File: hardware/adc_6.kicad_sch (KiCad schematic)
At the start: 14 parts, among them J5 Conn_01x04, U5 ADS122C04IPW

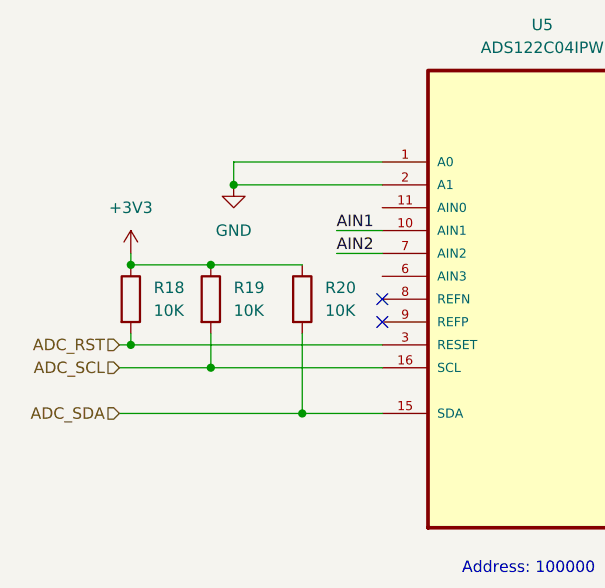
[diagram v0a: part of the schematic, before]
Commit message: Design Schematic for STM32F407
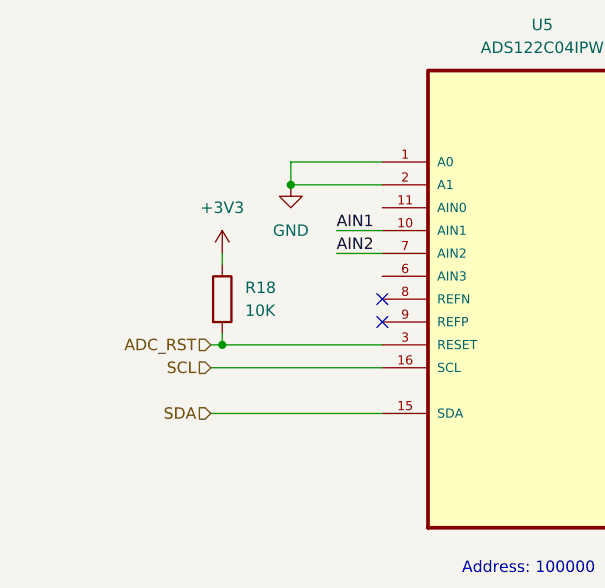
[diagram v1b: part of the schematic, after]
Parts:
- removed R19, R20: 10K, symbol Device:R
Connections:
- net ADC_SCL renamed SCL
- net ADC_SDA renamed SDA
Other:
- moved on the sheet: R18

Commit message: Complete Schematic for Power Section
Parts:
- renumbered C30 to C28, C31 to C29, C29 to C30, C32 to C31, C33 to C32, C34 to C33, R18 to R17, R21 to R18, R22 to R19
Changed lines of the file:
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@@
 		(dnp no)
 		(fields_autoplaced yes)
-		(property "Reference" "C31"
+		(property "Reference" "C29"
 			(at 176.53 100.3299 0)
 			(show_name no)
@@
 			(project "STM32F407 Dev Kit"
 				(path "/f3d27387-fbda-4c9d-aea0-93d92d34cd17/ffbc1d55-b358-41ae-b676-6d3702761bb2"
-					(reference "C31")
+					(reference "C29")
 					(unit 1)
 				)
@@
 		(dnp no)
 		(fields_autoplaced yes)
-		(property "Reference" "C33"
+		(property "Reference" "C32"
 			(at 199.39 109.2199 0)
 			(show_name no)
@@
 			(project "STM32F407 Dev Kit"
 				(path "/f3d27387-fbda-4c9d-aea0-93d92d34cd17/ffbc1d55-b358-41ae-b676-6d3702761bb2"
-					(reference "C33")
+					(reference "C32")
 					(unit 1)
 				)
@@
 		(dnp no)
 		(fields_autoplaced yes)
-		(property "Reference" "#PWR050"
+		(property "Reference" "#PWR051"
 			(at 165.1 87.63 0)
 			(hide yes)
@@
 			(project "STM32F407 Dev Kit"
 				(path "/f3d27387-fbda-4c9d-aea0-93d92d34cd17/ffbc1d55-b358-41ae-b676-6d3702761bb2"
-					(reference "#PWR050")
+					(reference "#PWR051")
 					(unit 1)
 				)
@@
 		(in_pos_files yes)
 		(dnp no)
-		(property "Reference" "R21"
+		(property "Reference" "R18"
 			(at 203.708 96.774 90)
 			(show_name no)
@@
 			(project "STM32F407 Dev Kit"
 				(path "/f3d27387-fbda-4c9d-aea0-93d92d34cd17/ffbc1d55-b358-41ae-b676-6d3702761bb2"
-					(reference "R21")
+					(reference "R18")
 					(unit 1)
 				)
@@
 		(dnp no)
 		(fields_autoplaced yes)
-		(property "Reference" "#PWR053"
+		(property "Reference" "#PWR048"
 			(at 149.86 120.65 0)
 			(hide yes)
@@
 			(project "STM32F407 Dev Kit"
 				(path "/f3d27387-fbda-4c9d-aea0-93d92d34cd17/ffbc1d55-b358-41ae-b676-6d3702761bb2"
-					(reference "#PWR053")
+					(reference "#PWR048")
 					(unit 1)
 				)
@@
 		(dnp no)
 		(fields_autoplaced yes)
-		(property "Reference" "#PWR034"
+		(property "Reference" "#PWR050"
 			(at 165.1 74.93 0)
 			(hide yes)
@@
 			(project "STM32F407 Dev Kit"
 				(path "/f3d27387-fbda-4c9d-aea0-93d92d34cd17/ffbc1d55-b358-41ae-b676-6d3702761bb2"
-					(reference "#PWR034")
+					(reference "#PWR050")
 					(unit 1)
 				)
@@
 		(dnp no)
 		(fields_autoplaced yes)
-		(property "Reference" "C29"
+		(property "Reference" "C30"
 			(at 177.8 62.2299 0)
 			(show_name no)
@@
 			(project "STM32F407 Dev Kit"
 				(path "/f3d27387-fbda-4c9d-aea0-93d92d34cd17/ffbc1d55-b358-41ae-b676-6d3702761bb2"
-					(reference "C29")
+					(reference "C30")
 					(unit 1)
 				)
@@
 		(dnp no)
 		(fields_autoplaced yes)
-		(property "Reference" "C30"
+		(property "Reference" "C28"
 			(at 168.91 74.9299 0)
 			(show_name no)
@@
 			(project "STM32F407 Dev Kit"
 				(path "/f3d27387-fbda-4c9d-aea0-93d92d34cd17/ffbc1d55-b358-41ae-b676-6d3702761bb2"
-					(reference "C30")
+					(reference "C28")
 					(unit 1)
 				)
@@
 		(dnp no)
 		(fields_autoplaced yes)
-		(property "Reference" "#PWR058"
+		(property "Reference" "#PWR053"
 			(at 184.15 121.92 0)
 			(hide yes)
@@
 			(project "STM32F407 Dev Kit"
 				(path "/f3d27387-fbda-4c9d-aea0-93d92d34cd17/ffbc1d55-b358-41ae-b676-6d3702761bb2"
-					(reference "#PWR058")
+					(reference "#PWR053")
 					(unit 1)
 				)
@@
 		(dnp no)
 		(fields_autoplaced yes)
-		(property "Reference" "#PWR052"
+		(property "Reference" "#PWR047"
 			(at 104.14 86.36 0)
 			(hide yes)
@@
 			(project "STM32F407 Dev Kit"
 				(path "/f3d27387-fbda-4c9d-aea0-93d92d34cd17/ffbc1d55-b358-41ae-b676-6d3702761bb2"
-					(reference "#PWR052")
+					(reference "#PWR047")
 					(unit 1)
 				)
@@
 		(dnp no)
 		(fields_autoplaced yes)
-		(property "Reference" "#PWR054"
+		(property "Reference" "#PWR046"
 			(at 96.52 91.44 0)
 			(hide yes)
@@
 			(project "STM32F407 Dev Kit"
 				(path "/f3d27387-fbda-4c9d-aea0-93d92d34cd17/ffbc1d55-b358-41ae-b676-6d3702761bb2"
-					(reference "#PWR054")
+					(reference "#PWR046")
 					(unit 1)
 				)
@@
 		(dnp no)
 		(fields_autoplaced yes)
-		(property "Reference" "#PWR059"
+		(property "Reference" "#PWR054"
 			(at 195.58 121.92 0)
 			(hide yes)
@@
 			(project "STM32F407 Dev Kit"
 				(path "/f3d27387-fbda-4c9d-aea0-93d92d34cd17/ffbc1d55-b358-41ae-b676-6d3702761bb2"
-					(reference "#PWR059")
+					(reference "#PWR054")
 					(unit 1)
 				)
@@
 		(in_pos_files yes)
 		(dnp no)
-		(property "Reference" "R22"
+		(property "Reference" "R19"
 			(at 203.708 104.14 90)
 			(show_name no)
@@
 			(project "STM32F407 Dev Kit"
 				(path "/f3d27387-fbda-4c9d-aea0-93d92d34cd17/ffbc1d55-b358-41ae-b676-6d3702761bb2"
-					(reference "R22")
+					(reference "R19")
 					(unit 1)
 				)
@@
 		(dnp no)
 		(fields_autoplaced yes)
-		(property "Reference" "C34"
+		(property "Reference" "C33"
 			(at 240.03 86.3599 0)
 			(show_name no)
@@
 			(project "STM32F407 Dev Kit"
 				(path "/f3d27387-fbda-4c9d-aea0-93d92d34cd17/ffbc1d55-b358-41ae-b676-6d3702761bb2"
-					(reference "C34")
+					(reference "C33")
 					(unit 1)
 				)
@@
 		(dnp no)
 		(fields_autoplaced yes)
-		(property "Reference" "#PWR051"
+		(property "Reference" "#PWR052"
 			(at 173.99 87.63 0)
 			(hide yes)
@@
 			(project "STM32F407 Dev Kit"
 				(path "/f3d27387-fbda-4c9d-aea0-93d92d34cd17/ffbc1d55-b358-41ae-b676-6d3702761bb2"
-					(reference "#PWR051")
+					(reference "#PWR052")
 					(unit 1)
 				)
@@
 		(dnp no)
 		(fields_autoplaced yes)
-		(property "Reference" "C32"
+		(property "Reference" "C31"
 			(at 187.96 109.2199 0)
 			(show_name no)
@@
 			(project "STM32F407 Dev Kit"
 				(path "/f3d27387-fbda-4c9d-aea0-93d92d34cd17/ffbc1d55-b358-41ae-b676-6d3702761bb2"
-					(reference "C32")
+					(reference "C31")
 					(unit 1)
 				)
@@
 		(dnp no)
 		(fields_autoplaced yes)
-		(property "Reference" "R18"
+		(property "Reference" "R17"
 			(at 99.06 91.4399 0)
 			(show_name no)
@@
 			(project "STM32F407 Dev Kit"
 				(path "/f3d27387-fbda-4c9d-aea0-93d92d34cd17/ffbc1d55-b358-41ae-b676-6d3702761bb2"
-					(reference "R18")
-					(unit 1)
-				)
+					(reference "R17")
+					(unit 1)
+				)

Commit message: Organize schematic
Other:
- note added: "ADC"
- note added: "Connector"
- moved on the sheet: C28, C29, C30, C31, C32, C33, FB2, J5, R17, R18, R19, U5

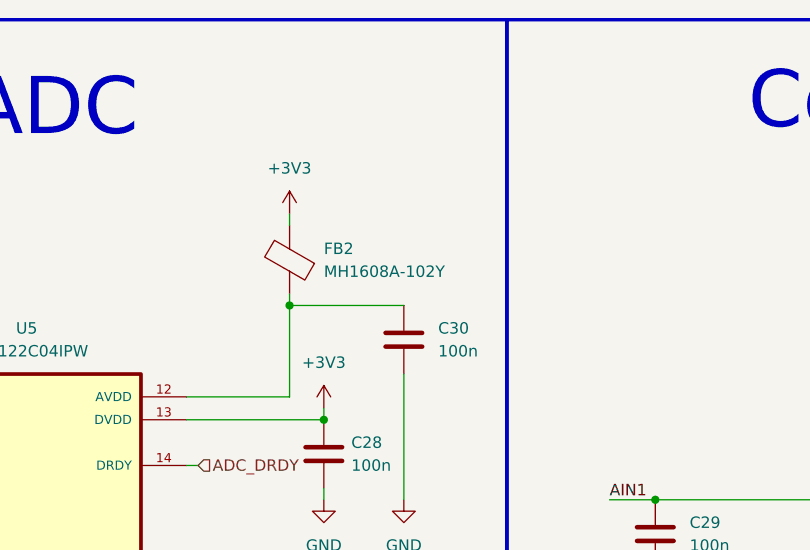
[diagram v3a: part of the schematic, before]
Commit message: Link footprints to Symbols
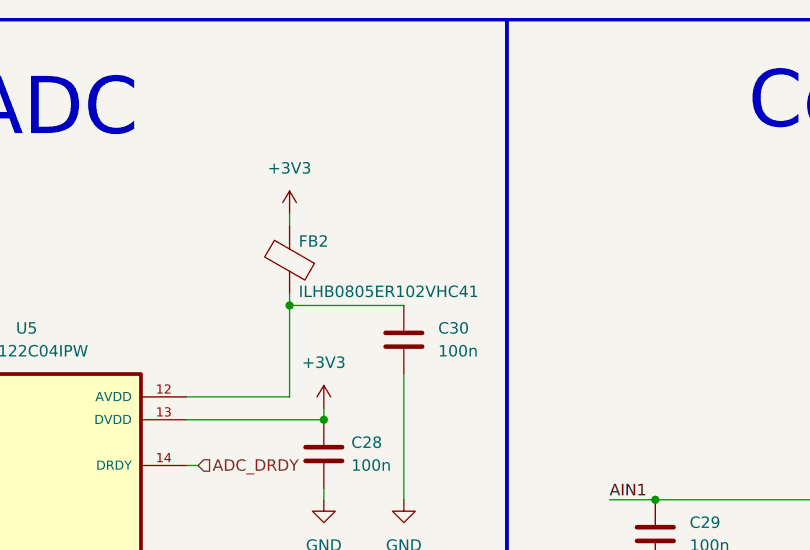
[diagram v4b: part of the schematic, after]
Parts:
- C28, C29, C30, C31, C32, C33: footprint (none) -> STM32F407 Dev Kit Library:C_0805_2012Metric_Pad1.18x1.45mm_HandSolder
- FB2: value MH1608A-102Y -> ILHB0805ER102VHC41; footprint Package_LCC:PLCC-84_29.3x29.3mm_P1.27mm -> STM32F407 Dev Kit Library:C_0805_2012Metric_Pad1.18x1.45mm_HandSolder
- J5: footprint Connector_RJ:RJ45_Abracon_ARJP11A-MA_Horizontal -> STM32F407 Dev Kit Library:PinHeader_1x04_P2.54mm_Vertical
- R17, R18, R19: footprint (none) -> STM32F407 Dev Kit Library:R_0805_2012Metric_Pad1.20x1.40mm_HandSolder
- U5: footprint ADS122C04IPW:SOP65P640X120-16N -> STM32F407 Dev Kit Library:TSSOP-16_4.4x5mm_P0.65mm
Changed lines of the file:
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@@
 			)
 		)
-		(property "Footprint" ""
+		(property "Footprint" "STM32F407 Dev Kit Library:C_0805_2012Metric_Pad1.18x1.45mm_HandSolder"
 			(at 169.8752 102.87 0)
 			(hide yes)
@@
 			)
 		)
-		(property "Footprint" ""
+		(property "Footprint" "STM32F407 Dev Kit Library:C_0805_2012Metric_Pad1.18x1.45mm_HandSolder"
 			(at 192.7352 111.76 0)
 			(hide yes)
@@
 			)
 		)
-		(property "Footprint" ""
+		(property "Footprint" "STM32F407 Dev Kit Library:R_0805_2012Metric_Pad1.20x1.40mm_HandSolder"
 			(at 204.47 97.028 90)
 			(hide yes)
@@
 			)
 		)
-		(property "Footprint" ""
+		(property "Footprint" "STM32F407 Dev Kit Library:C_0805_2012Metric_Pad1.18x1.45mm_HandSolder"
 			(at 141.9352 81.28 0)
 			(hide yes)
@@
 			)
 		)
-		(property "Footprint" ""
+		(property "Footprint" "STM32F407 Dev Kit Library:C_0805_2012Metric_Pad1.18x1.45mm_HandSolder"
 			(at 133.0452 93.98 0)
 			(hide yes)
@@
 		(in_pos_files yes)
 		(dnp no)
-		(fields_autoplaced yes)
 		(property "Reference" "FB2"
-			(at 132.08 67.3607 0)
+			(at 129.286 66.548 0)
 			(show_name no)
 			(do_not_autoplace no)
@@
 			)
 		)
-		(property "Value" "MH1608A-102Y"
-			(at 132.08 69.9007 0)
+		(property "Value" "ILHB0805ER102VHC41"
+			(at 129.286 72.136 0)
 			(show_name no)
 			(do_not_autoplace no)
@@
 			)
 		)
-		(property "Footprint" "Package_LCC:PLCC-84_29.3x29.3mm_P1.27mm"
+		(property "Footprint" "STM32F407 Dev Kit Library:C_0805_2012Metric_Pad1.18x1.45mm_HandSolder"
 			(at 130.048 68.58 90)
 			(hide yes)
@@
 			)
 		)
-		(property "Footprint" "ADS122C04IPW:SOP65P640X120-16N"
+		(property "Footprint" "STM32F407 Dev Kit Library:TSSOP-16_4.4x5mm_P0.65mm"
 			(at 99.06 106.68 0)
 			(hide yes)
@@
 			)
 		)
-		(property "Footprint" ""
+		(property "Footprint" "STM32F407 Dev Kit Library:R_0805_2012Metric_Pad1.20x1.40mm_HandSolder"
 			(at 204.47 104.648 90)
 			(hide yes)
@@
 			)
 		)
-		(property "Footprint" ""
+		(property "Footprint" "STM32F407 Dev Kit Library:C_0805_2012Metric_Pad1.18x1.45mm_HandSolder"
 			(at 233.3752 88.9 0)
 			(hide yes)
@@
 			)
 		)
-		(property "Footprint" "Connector_RJ:RJ45_Abracon_ARJP11A-MA_Horizontal"
+		(property "Footprint" "STM32F407 Dev Kit Library:PinHeader_1x04_P2.54mm_Vertical"
 			(at 227.33 97.79 0)
 			(hide yes)
@@
 			)
 		)
-		(property "Footprint" ""
+		(property "Footprint" "STM32F407 Dev Kit Library:C_0805_2012Metric_Pad1.18x1.45mm_HandSolder"
 			(at 181.3052 111.76 0)
 			(hide yes)
@@
 			)
 		)
-		(property "Footprint" ""
+		(property "Footprint" "STM32F407 Dev Kit Library:R_0805_2012Metric_Pad1.20x1.40mm_HandSolder"
 			(at 61.722 106.68 90)
 			(hide yes)

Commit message: Convert Schematic to PCB
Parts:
- renumbered C30 to C29, C29 to C30
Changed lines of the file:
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@@
 		(dnp no)
 		(fields_autoplaced yes)
-		(property "Reference" "C29"
+		(property "Reference" "C30"
 			(at 172.72 97.7899 0)
 			(show_name no)
@@
 			(project "STM32F407 Dev Kit"
 				(path "/f3d27387-fbda-4c9d-aea0-93d92d34cd17/ffbc1d55-b358-41ae-b676-6d3702761bb2"
-					(reference "C29")
+					(reference "C30")
 					(unit 1)
 				)
@@
 		(dnp no)
 		(fields_autoplaced yes)
-		(property "Reference" "#PWR051"
+		(property "Reference" "#PWR056"
 			(at 132.08 101.6 0)
 			(hide yes)
@@
 			(project "STM32F407 Dev Kit"
 				(path "/f3d27387-fbda-4c9d-aea0-93d92d34cd17/ffbc1d55-b358-41ae-b676-6d3702761bb2"
-					(reference "#PWR051")
+					(reference "#PWR056")
 					(unit 1)
 				)
@@
 		(dnp no)
 		(fields_autoplaced yes)
-		(property "Reference" "#PWR048"
+		(property "Reference" "#PWR053"
 			(at 116.84 134.62 0)
 			(hide yes)
@@
 			(project "STM32F407 Dev Kit"
 				(path "/f3d27387-fbda-4c9d-aea0-93d92d34cd17/ffbc1d55-b358-41ae-b676-6d3702761bb2"
-					(reference "#PWR048")
+					(reference "#PWR053")
 					(unit 1)
 				)
@@
 		(dnp no)
 		(fields_autoplaced yes)
-		(property "Reference" "#PWR049"
+		(property "Reference" "#PWR054"
 			(at 128.27 67.31 0)
 			(hide yes)
@@
 			(project "STM32F407 Dev Kit"
 				(path "/f3d27387-fbda-4c9d-aea0-93d92d34cd17/ffbc1d55-b358-41ae-b676-6d3702761bb2"
-					(reference "#PWR049")
+					(reference "#PWR054")
 					(unit 1)
 				)
@@
 		(dnp no)
 		(fields_autoplaced yes)
-		(property "Reference" "#PWR050"
+		(property "Reference" "#PWR055"
 			(at 132.08 88.9 0)
 			(hide yes)
@@
 			(project "STM32F407 Dev Kit"
 				(path "/f3d27387-fbda-4c9d-aea0-93d92d34cd17/ffbc1d55-b358-41ae-b676-6d3702761bb2"
-					(reference "#PWR050")
+					(reference "#PWR055")
 					(unit 1)
 				)
@@
 		(dnp no)
 		(fields_autoplaced yes)
-		(property "Reference" "#PWR057"
+		(property "Reference" "#PWR062"
 			(at 232.41 96.52 0)
 			(hide yes)
@@
 			(project "STM32F407 Dev Kit"
 				(path "/f3d27387-fbda-4c9d-aea0-93d92d34cd17/ffbc1d55-b358-41ae-b676-6d3702761bb2"
-					(reference "#PWR057")
+					(reference "#PWR062")
 					(unit 1)
 				)
@@
 		(dnp no)
 		(fields_autoplaced yes)
-		(property "Reference" "C30"
+		(property "Reference" "C29"
 			(at 144.78 76.1999 0)
 			(show_name no)
@@
 			(project "STM32F407 Dev Kit"
 				(path "/f3d27387-fbda-4c9d-aea0-93d92d34cd17/ffbc1d55-b358-41ae-b676-6d3702761bb2"
-					(reference "C30")
+					(reference "C29")
 					(unit 1)
 				)
@@
 		(dnp no)
 		(fields_autoplaced yes)
-		(property "Reference" "#PWR053"
+		(property "Reference" "#PWR058"
 			(at 180.34 119.38 0)
 			(hide yes)
@@
 			(project "STM32F407 Dev Kit"
 				(path "/f3d27387-fbda-4c9d-aea0-93d92d34cd17/ffbc1d55-b358-41ae-b676-6d3702761bb2"
-					(reference "#PWR053")
+					(reference "#PWR058")
 					(unit 1)
 				)
@@
 		(dnp no)
 		(fields_autoplaced yes)
-		(property "Reference" "#PWR047"
+		(property "Reference" "#PWR052"
 			(at 71.12 100.33 0)
 			(hide yes)
@@
 			(project "STM32F407 Dev Kit"
 				(path "/f3d27387-fbda-4c9d-aea0-93d92d34cd17/ffbc1d55-b358-41ae-b676-6d3702761bb2"
-					(reference "#PWR047")
+					(reference "#PWR052")
 					(unit 1)
 				)
@@
 		(dnp no)
 		(fields_autoplaced yes)
-		(property "Reference" "#PWR046"
+		(property "Reference" "#PWR051"
 			(at 63.5 105.41 0)
 			(hide yes)
@@
 			(project "STM32F407 Dev Kit"
 				(path "/f3d27387-fbda-4c9d-aea0-93d92d34cd17/ffbc1d55-b358-41ae-b676-6d3702761bb2"
-					(reference "#PWR046")
+					(reference "#PWR051")
 					(unit 1)
 				)
@@
 		(dnp no)
 		(fields_autoplaced yes)
-		(property "Reference" "#PWR056"
+		(property "Reference" "#PWR061"
 			(at 222.25 119.38 0)
 			(hide yes)
@@
 			(project "STM32F407 Dev Kit"
 				(path "/f3d27387-fbda-4c9d-aea0-93d92d34cd17/ffbc1d55-b358-41ae-b676-6d3702761bb2"
-					(reference "#PWR056")
+					(reference "#PWR061")
 					(unit 1)
 				)
@@
 		(dnp no)
 		(fields_autoplaced yes)
-		(property "Reference" "#PWR054"
+		(property "Reference" "#PWR059"
 			(at 191.77 119.38 0)
 			(hide yes)
@@
 			(project "STM32F407 Dev Kit"
 				(path "/f3d27387-fbda-4c9d-aea0-93d92d34cd17/ffbc1d55-b358-41ae-b676-6d3702761bb2"
-					(reference "#PWR054")
+					(reference "#PWR059")
 					(unit 1)
 				)
@@
 		(dnp no)
 		(fields_autoplaced yes)
-		(property "Reference" "#PWR055"
+		(property "Reference" "#PWR060"
 			(at 222.25 83.82 0)
 			(hide yes)
@@
 			(project "STM32F407 Dev Kit"
 				(path "/f3d27387-fbda-4c9d-aea0-93d92d34cd17/ffbc1d55-b358-41ae-b676-6d3702761bb2"
-					(reference "#PWR055")
+					(reference "#PWR060")
 					(unit 1)
 				)
@@
 		(dnp no)
 		(fields_autoplaced yes)
-		(property "Reference" "#PWR052"
+		(property "Reference" "#PWR057"
 			(at 140.97 101.6 0)
 			(hide yes)
@@
 			(project "STM32F407 Dev Kit"
 				(path "/f3d27387-fbda-4c9d-aea0-93d92d34cd17/ffbc1d55-b358-41ae-b676-6d3702761bb2"
-					(reference "#PWR052")
-					(unit 1)
-				)
+					(reference "#PWR057")
+					(unit 1)
+				)

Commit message: Place components for ADC
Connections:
- net AIN1: now also C30.2, C31.1, R19.1; no longer C30.1, C32.1, R18.1
- net AIN2: now also C30.1, C32.1, R18.1; no longer C30.2, C31.1, R19.1
- net SENSOR_PIN1: now also J5.3 (Pin_3), R19.2; no longer J5.2 (Pin_2), R18.2
- net SENSOR_PIN2: now also J5.2 (Pin_2), R18.2; no longer J5.3 (Pin_3), R19.2
- no-connect marks 2 -> 4
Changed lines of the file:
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@@
+	)
+	(no_connect
+		(at 81.28 96.52)
+	)
+	(no_connect
+		(at 81.28 104.14)
 	)
 	(no_connect
@@
 		)
 	)
-	(label "SENSOR_PIN2"
-		(at 208.28 100.33 0)
+	(label "AIN2"
+		(at 163.83 95.25 0)
 		(effects
 			(font
@@
 		)
 	)
-	(label "AIN2"
-		(at 76.2 101.6 0)
+	(label "AIN1"
+		(at 163.83 102.87 0)
 		(effects
 			(font
@@
 		)
 	)
-	(label "AIN1"
-		(at 76.2 99.06 0)
+	(label "SENSOR_PIN1"
+		(at 208.28 100.33 0)
 		(effects
 			(font
@@
 		)
 	)
-	(label "AIN1"
-		(at 163.83 95.25 0)
+	(label "AIN2"
+		(at 76.2 101.6 0)
 		(effects
 			(font
@@
 		)
 	)
-	(label "SENSOR_PIN1"
-		(at 208.28 97.79 0)
+	(label "AIN1"
+		(at 76.2 99.06 0)
 		(effects
 			(font
@@
 		)
 	)
-	(label "AIN2"
-		(at 163.83 102.87 0)
-		(effects
-			(font
+	(label "SENSOR_PIN2"
+		(at 208.28 97.79 0)
+		(effects
+			(font
